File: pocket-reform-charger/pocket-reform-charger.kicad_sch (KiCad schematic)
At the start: 63 parts, among them J1 CHARGER, Q1 IRF7458TRPBF, Q2 IRF7458TRPBF, U1 MP2650, U2 MAX17320G20+

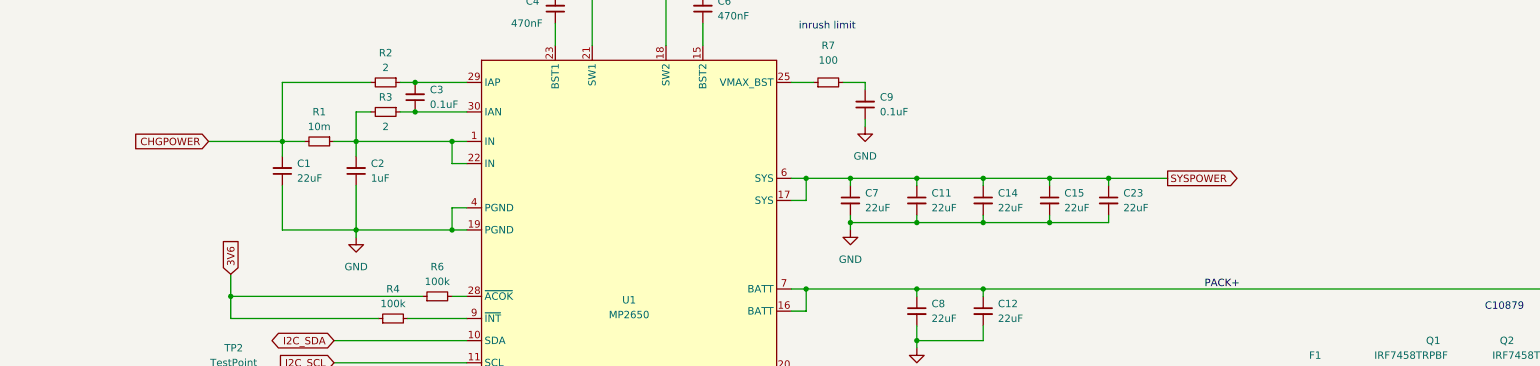
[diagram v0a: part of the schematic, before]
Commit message: charger: v2 WIP
* new 4 layer design
* optimized current flow
* better sense layout
* actually have smth worthy of being called a ground plane

missing:
* NX20P5090UKAZ
* routing of I/O signals
* proper kelvin footprint
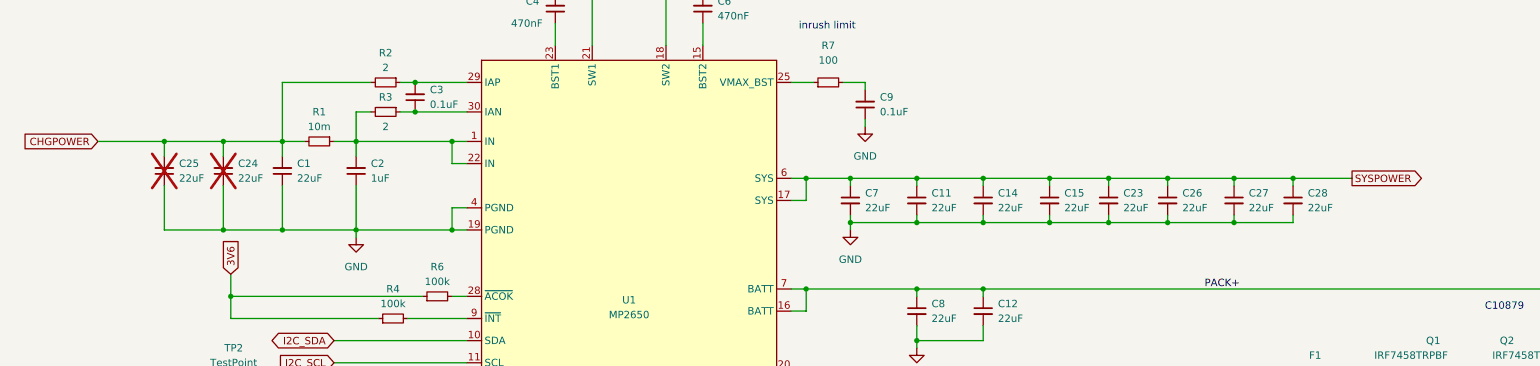
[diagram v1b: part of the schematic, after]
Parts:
- added C24, C25, C26, C27, C28: 22uF, Capacitor_SMD:C_0805_2012Metric, symbol Device:C_Small
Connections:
- net CHGPOWER: now also C24.2, C25.2
- net GND: now also C24.1, C25.1, C26.2, C27.2, C28.2
- net SYSPOWER: now also C26.1, C27.1, C28.1

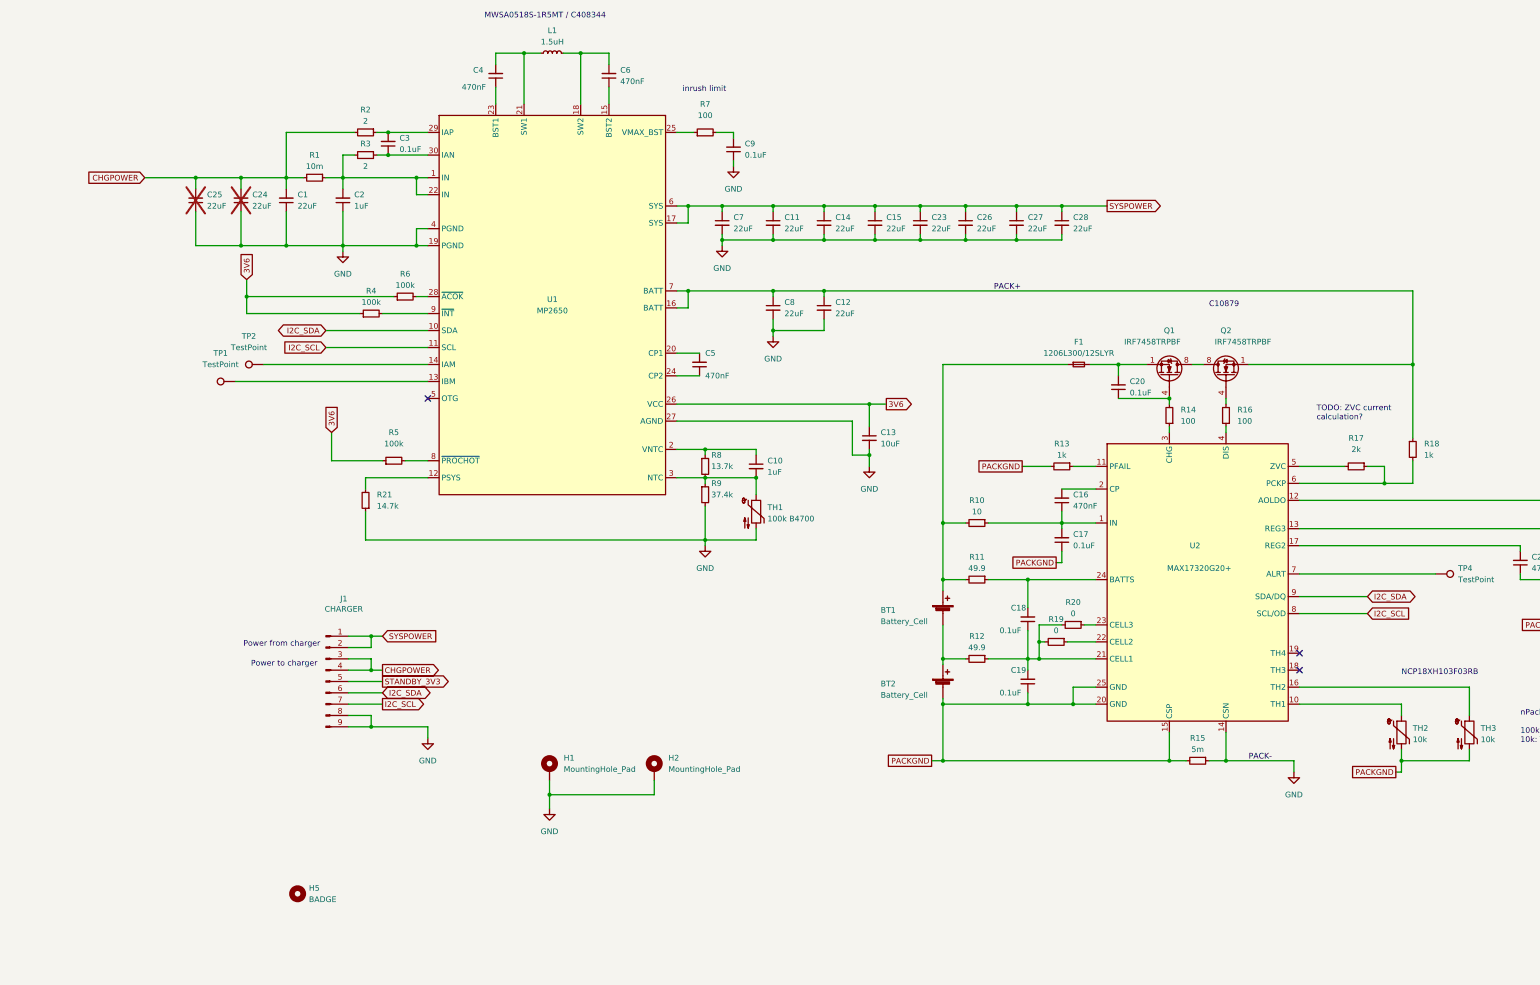
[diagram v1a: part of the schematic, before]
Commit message: charger: v2 WIP
* changed IRF FETs to cheaper diodes dual FET
* Add NXP 20P5090 OVP / slew rate limiter

missing:
* SYSPOWER routing to J1
* I2C, NTC filtering
* review of MAX17320G20+ protection layout
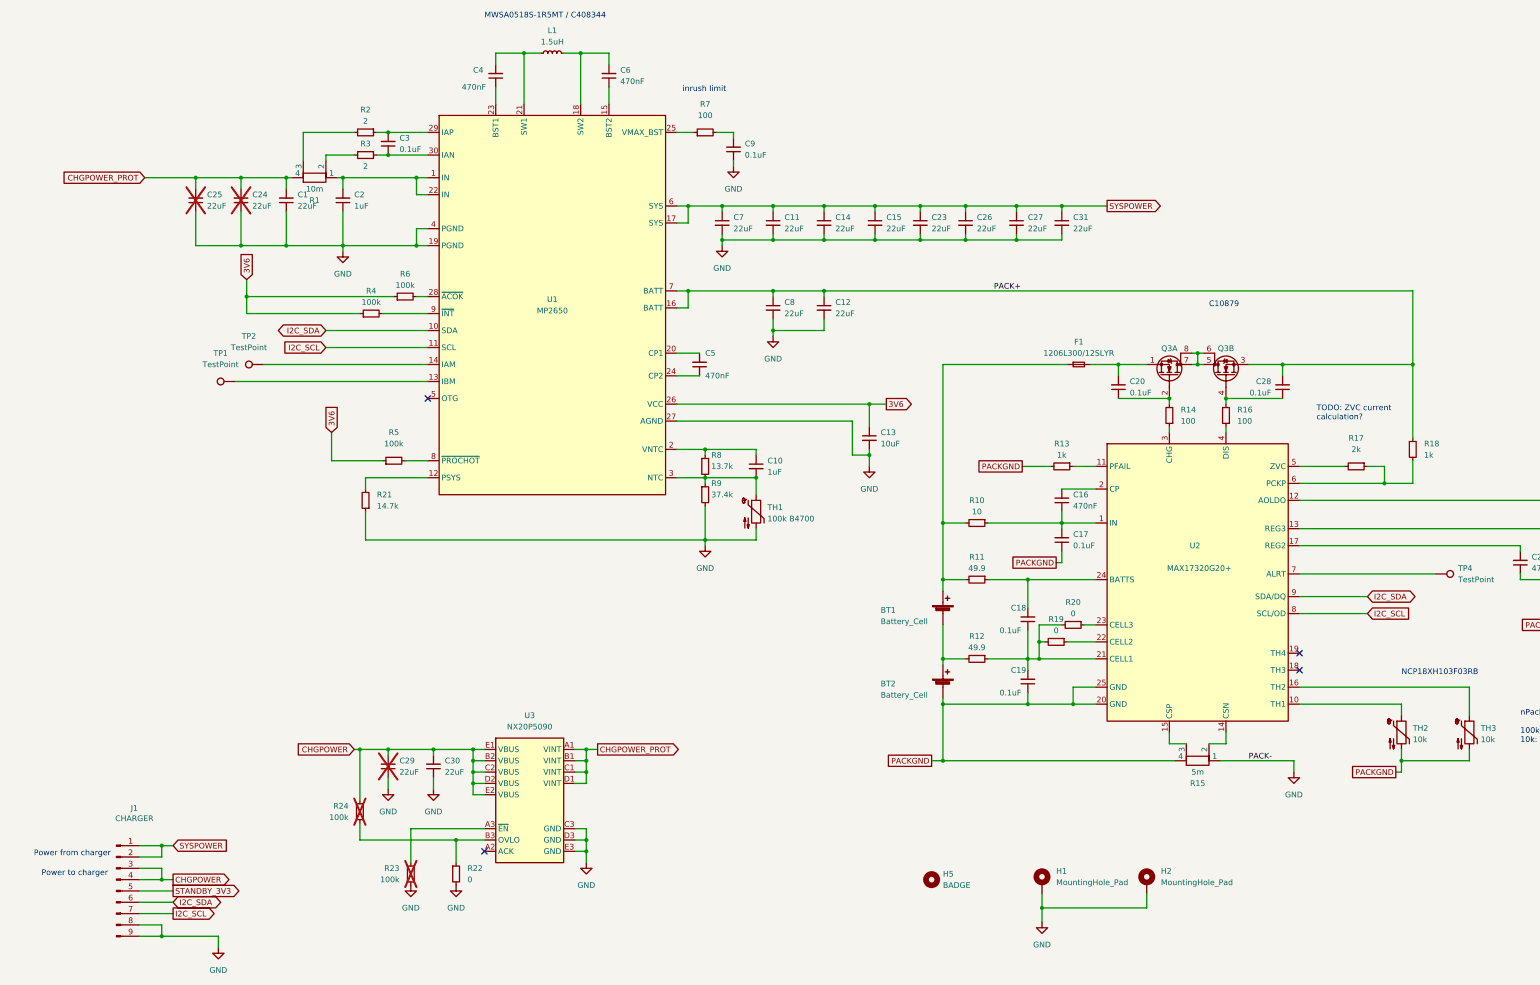
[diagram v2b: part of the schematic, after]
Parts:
- removed Q1, Q2: IRF7458TRPBF, Package_SO:SOIC-8_3.9x4.9mm_P1.27mm, symbol Transistor_FET:IRF7403
- added C29, C30, C31: 22uF, Capacitor_SMD:C_0805_2012Metric, symbol Device:C_Small
- added Q3: Q_Dual_NMOS_S1G1S2G2D2D2D1D1, Package_SO:SOIC-8_3.9x4.9mm_P1.27mm, symbol Device:Q_Dual_NMOS_S1G1S2G2D2D2D1D1
- added R22: 0, Resistor_SMD:R_0603_1608Metric, symbol Device:R_Small
- added R23, R24: 100k, Resistor_SMD:R_0603_1608Metric, symbol Device:R_Small
- added U3: NX20P5090, pocket-reform-charger:NXP_NX20P5090, symbol pocket-reform-charger:NX20P5090
- C28: value 22uF -> 0.1uF; footprint Capacitor_SMD:C_0805_2012Metric -> Capacitor_SMD:C_0603_1608Metric; LCSC C86816 -> C385964; Manufacturer Murata -> Taiyo Yuden; Manufacturer_No GRM21BR61E226ME44L -> GMK107B7104KAHT
- R1, R15: footprint Resistor_SMD:R_1206_3216Metric -> pocket-reform-charger:R_1206_3216Metric_Kelvin; symbol Device:R_Small -> Device:R_Shunt
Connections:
- net CHGPOWER: now also C29.2, C30.2, R24.2, U3.B2 (VBUS), U3.C2 (VBUS), U3.D2 (VBUS), U3.E1 (VBUS), U3.E2 (VBUS); no longer C1.2, C24.2, C25.2, R1.2, R2.2
- net GND: now also C29.1, C30.1, C31.2, R22.2, R23.1, U3.C3 (GND), U3.D3 (GND), U3.E3 (GND); no longer C28.2, U2.14 (CSN)
- net PACK+: now also C28.2, Q3.3 (S)
- net PACKGND: now also R15.4; no longer R15.2, U2.15 (CSP)
- net SYSPOWER: now also C31.1; no longer C28.1
- net at C2.2, R1.1, U1.1 (IN)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: no longer R3.2
- net at C20.2, F1.2: now also Q3.1 (S)
- net at R16.2: now also C28.1, Q3.4 (G)
- net at C20.1, R14.2: now also Q3.2 (G)
- new net: R23.2, U3.A3 (~{EN})
- new net: R22.1, R24.1, U3.B3 (OVLO)
- new net: R1.2, R3.2
- new net: R1.3, R2.2
- new net: R15.2, U2.14 (CSN)
- new net: R15.3, U2.15 (CSP)
- new net: Q3.5 (D), Q3.6 (D), Q3.7 (D), Q3.8 (D)
- new net CHGPOWER_PROT: C1.2, C24.2, C25.2, R1.4, U3.A1 (VINT), U3.B1 (VINT), U3.C1 (VINT), U3.D1 (VINT)
- no-connect marks 3 -> 4
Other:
- moved on the sheet: H1, H2, H5, J1

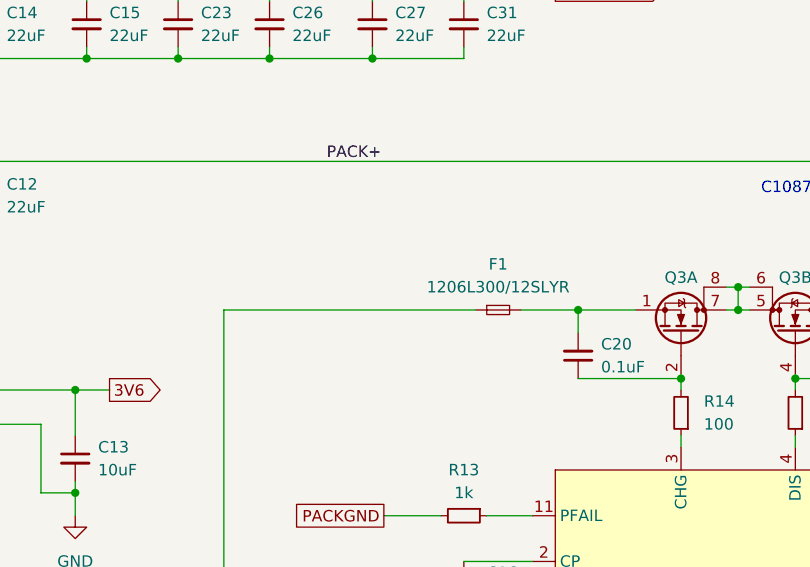
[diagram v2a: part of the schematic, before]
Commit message: pocket-reform-charger pcb v2 layout completed
- layout finished by carson walls
- initial new mp2650+nx20p5090 layout by f. schneider
- final polishing by lucie l. hartmann

Co-authored-by: Carson Walls <carson@decapoddevices.com>
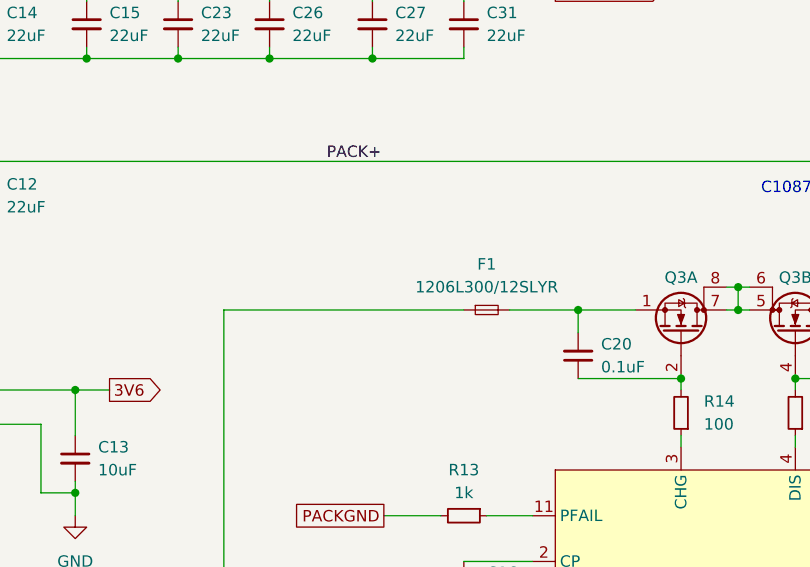
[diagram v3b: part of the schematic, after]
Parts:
- R11, R12: footprint Resistor_SMD:R_0603_1608Metric -> Resistor_SMD:R_1206_3216Metric; LCSC C403255 -> C4014562; Manufacturer Panasonic -> VISHAY; Manufacturer_No ERJ3EKF49R9V -> CRCW120649R9FKEAHP
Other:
- moved on the sheet: F1
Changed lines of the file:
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@@
 	(wire
 		(pts
+			(xy 227.33 142.24) (xy 254 142.24)
+		)
+		(stroke
+			(width 0)
+			(type default)
+		)
+	)
+	(wire
+		(pts
 			(xy 167.64 154.94) (xy 207.01 154.94)
 		)
@@
 	(wire
 		(pts
-			(xy 260.35 142.24) (xy 266.7 142.24)
+			(xy 259.08 142.24) (xy 266.7 142.24)
 		)
 		(stroke
@@
 	(wire
 		(pts
-			(xy 255.27 142.24) (xy 227.33 142.24)
-		)
-		(stroke
-			(width 0)
-			(type default)
-		)
-	)
-	(wire
-		(pts
 			(xy 144.78 228.6) (xy 147.32 228.6)
 		)
@@
 	(symbol
 		(lib_id "Device:Fuse_Small")
-		(at 257.81 142.24 0)
+		(at 256.54 142.24 0)
 		(unit 1)
 		(exclude_from_sim no)
@@
 		(fields_autoplaced yes)
 		(property "Reference" "F1"
-			(at 257.81 137.16 0)
+			(at 256.54 137.16 0)
 			(effects
 				(font
@@
 		)
 		(property "Value" "1206L300/12SLYR"
-			(at 257.81 139.7 0)
+			(at 256.54 139.7 0)
 			(effects
 				(font
@@
 		)
 		(property "Footprint" "Fuse:Fuse_1206_3216Metric"
-			(at 257.81 142.24 0)
+			(at 256.54 142.24 0)
 			(effects
 				(font
@@
 		)
 		(property "Datasheet" "~"
-			(at 257.81 142.24 0)
+			(at 256.54 142.24 0)
 			(effects
 				(font
@@
 		)
 		(property "Description" ""
-			(at 257.81 142.24 0)
+			(at 256.54 142.24 0)
 			(effects
 				(font
@@
 		)
 		(property "LCSC" "C1512043"
-			(at 257.81 142.24 0)
+			(at 256.54 142.24 0)
 			(effects
 				(font
@@
 		)
 		(property "Manufacturer" "Littelfuse"
-			(at 257.81 142.24 0)
+			(at 256.54 142.24 0)
 			(effects
 				(font
@@
 		)
 		(property "Manufacturer_No" "1206L300/12SLYR"
-			(at 257.81 142.24 0)
+			(at 256.54 142.24 0)
 			(effects
 				(font
@@
 			)
 		)
-		(property "Footprint" "Resistor_SMD:R_0603_1608Metric"
+		(property "Footprint" "Resistor_SMD:R_1206_3216Metric"
 			(at 234.95 190.5 0)
 			(effects
@@
 			)
 		)
-		(property "LCSC" "C403255"
+		(property "LCSC" "C4014562"
 			(at 234.95 190.5 0)
 			(effects
@@
 			)
 		)
-		(property "Manufacturer" "Panasonic"
+		(property "Manufacturer" "VISHAY"
 			(at 234.95 190.5 0)
 			(effects
@@
 			)
 		)
-		(property "Manufacturer_No" "ERJ3EKF49R9V"
+		(property "Manufacturer_No" "CRCW120649R9FKEAHP"
 			(at 234.95 190.5 0)
 			(effects
@@
 			)
 		)
-		(property "Footprint" "Resistor_SMD:R_0603_1608Metric"
+		(property "Footprint" "Resistor_SMD:R_1206_3216Metric"
 			(at 234.95 208.28 0)
 			(effects
@@
 			)
 		)
-		(property "LCSC" "C403255"
+		(property "LCSC" "C4014562"
 			(at 234.95 208.28 0)
 			(effects
@@
 			)
 		)
-		(property "Manufacturer" "Panasonic"
+		(property "Manufacturer" "VISHAY"
 			(at 234.95 208.28 0)
 			(effects
@@
 			)
 		)
-		(property "Manufacturer_No" "ERJ3EKF49R9V"
+		(property "Manufacturer_No" "CRCW120649R9FKEAHP "
 			(at 234.95 208.28 0)
 			(effects
